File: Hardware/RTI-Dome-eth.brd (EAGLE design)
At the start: 119.4 x 71.1 mm, 87 parts, among them IC1 24AA128ST, IC3 FT232RL, IC4 REG1117, IC5 74LVC245, IC6 74ABT245, J1 POWERPOLE_POWER45A, U1 W5500, X13 PN61729-S, X9 J1011F21PNL

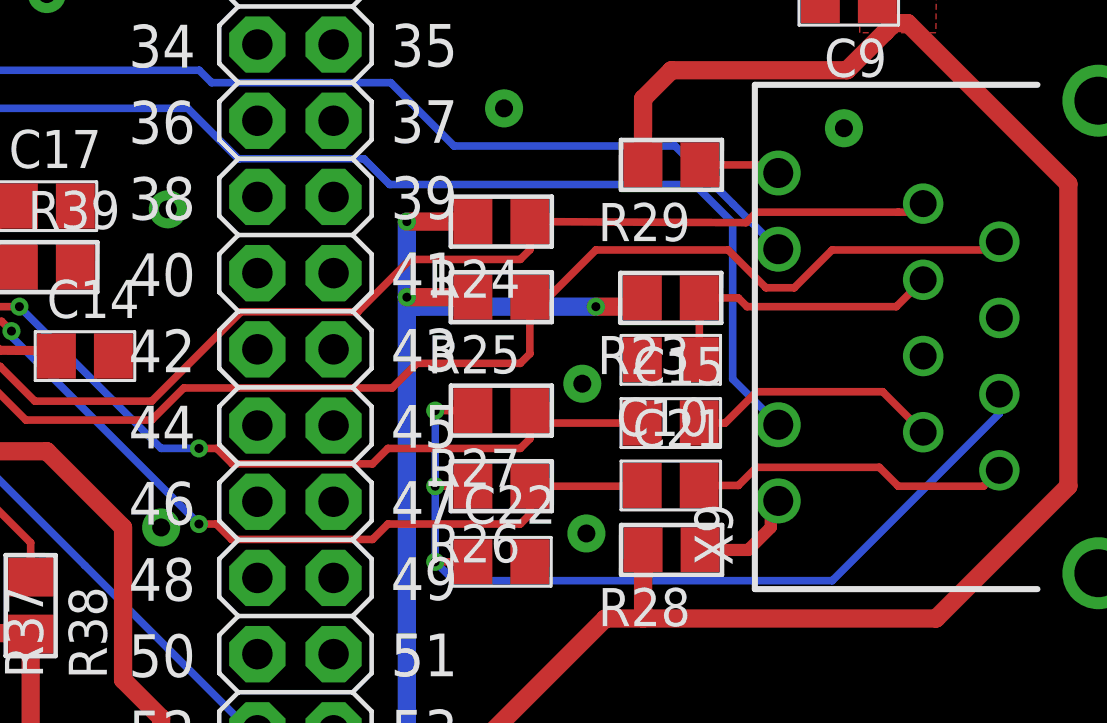
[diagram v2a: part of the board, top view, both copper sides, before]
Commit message: Differential pair are now closer to be the same length.
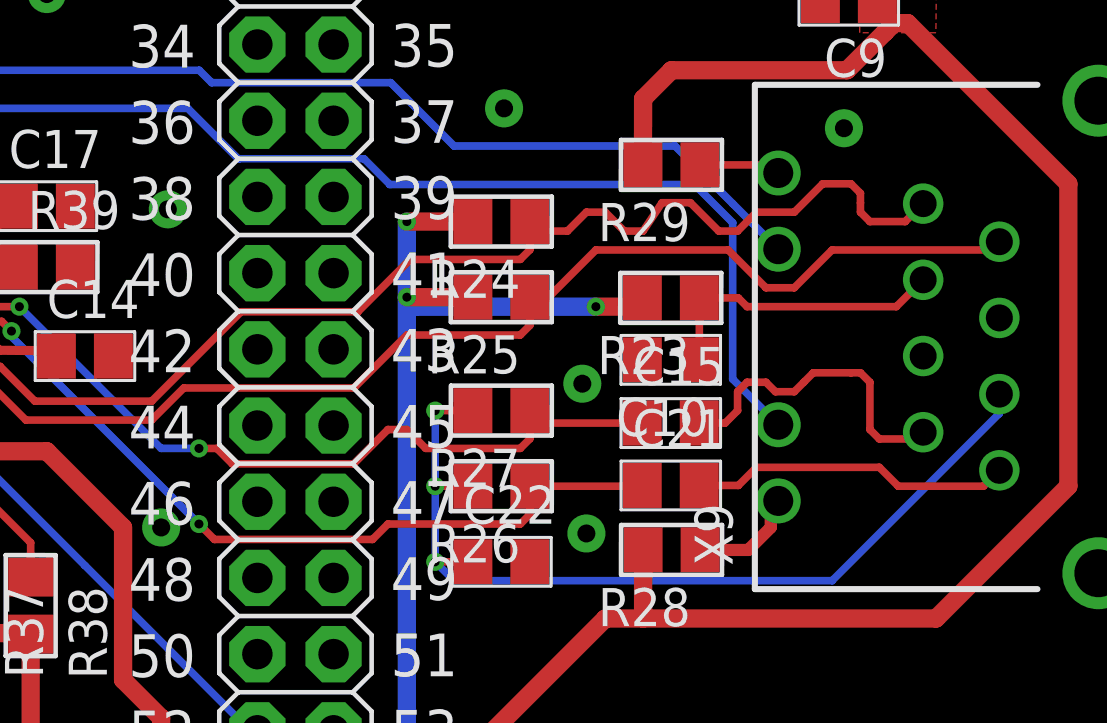
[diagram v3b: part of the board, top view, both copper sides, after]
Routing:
- net TXP: track 36.4 -> 39.4 mm
- net N$11: track 8.46 -> 10.7 mm
- net TXN: track 40.3 -> 39.7 mm
- net RXP: track 26.8 -> 27.4 mm
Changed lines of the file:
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@@
 <wire x1="102.375" y1="34.65" x2="107.675" y2="34.65" width="0.254" layer="1"/>
 <wire x1="107.675" y1="34.65" x2="107.95" y2="34.925" width="0.254" layer="1"/>
-<wire x1="92.3" y1="33.075" x2="92.3" y2="31.19" width="0.254" layer="1"/>
-<wire x1="92.3" y1="31.19" x2="91.98" y2="30.87" width="0.254" layer="1"/>
-<wire x1="91.98" y1="30.87" x2="88.53" y2="30.87" width="0.254" layer="1"/>
-<wire x1="88.53" y1="30.87" x2="87.71" y2="30.05" width="0.254" layer="1"/>
-<wire x1="87.71" y1="30.05" x2="80.765" y2="30.05" width="0.254" layer="1"/>
+<wire x1="86.45" y1="30.05" x2="80.765" y2="30.05" width="0.254" layer="1"/>
 <wire x1="80.765" y1="30.05" x2="79.695" y2="28.98" width="0.254" layer="1"/>
 <wire x1="79.695" y1="28.98" x2="75.5" y2="28.98" width="0.254" layer="1"/>
@@
 <wire x1="74.23" y1="30.25" x2="72.85" y2="30.25" width="0.254" layer="1"/>
 <wire x1="72.85" y1="30.25" x2="72.83" y2="30.27" width="0.254" layer="1"/>
+<wire x1="92.3" y1="33.075" x2="92.3" y2="32.135" width="0.254" layer="1"/>
+<wire x1="92.3" y1="32.135" x2="91.98" y2="31.815" width="0.254" layer="1"/>
+<wire x1="91.98" y1="31.815" x2="88.2" y2="31.815" width="0.254" layer="1"/>
+<wire x1="86.45" y1="30.05" x2="86.45" y2="30.065" width="0.254" layer="1"/>
+<wire x1="86.45" y1="30.065" x2="88.2" y2="31.815" width="0.254" layer="1"/>
 </signal>
 <signal name="RXP">
@@
 <wire x1="92.3" y1="29.295" x2="92.3" y2="28.355" width="0.254" layer="1"/>
 <wire x1="92.3" y1="28.355" x2="91.98" y2="28.035" width="0.254" layer="1"/>
-<wire x1="91.98" y1="28.035" x2="87.57" y2="28.035" width="0.254" layer="1"/>
 <via x="81.27" y="28.035" extent="1-16" drill="0.3"/>
 <wire x1="81.27" y1="28.035" x2="80.01" y2="28.035" width="0.254" layer="16"/>
@@
 <wire x1="75.285" y1="32.76" x2="72.84" y2="32.76" width="0.254" layer="1"/>
 <wire x1="72.84" y1="32.76" x2="72.83" y2="32.77" width="0.254" layer="1"/>
-<wire x1="87.57" y1="28.035" x2="87.055" y2="27.52" width="0.254" layer="1"/>
-<wire x1="87.055" y1="27.52" x2="82.38" y2="27.52" width="0.254" layer="1"/>
+<wire x1="86.425" y1="27.52" x2="82.38" y2="27.52" width="0.254" layer="1"/>
 <wire x1="82.38" y1="27.52" x2="81.865" y2="28.035" width="0.254" layer="1"/>
 <wire x1="81.865" y1="28.035" x2="81.27" y2="28.035" width="0.254" layer="1"/>
+<wire x1="86.425" y1="27.52" x2="87.57" y2="28.665" width="0.254" layer="1"/>
+<wire x1="87.57" y1="28.665" x2="88.2" y2="28.665" width="0.254" layer="1"/>
+<wire x1="88.2" y1="28.665" x2="88.83" y2="28.035" width="0.254" layer="1"/>
+<wire x1="88.83" y1="28.035" x2="91.98" y2="28.035" width="0.254" layer="1"/>
 </signal>
 <signal name="RXN">
@@
 <wire x1="87.57" y1="25.515" x2="87.055" y2="25" width="0.254" layer="1"/>
 <wire x1="87.055" y1="25" x2="82.36" y2="25" width="0.254" layer="1"/>
-<wire x1="82.36" y1="25" x2="81.845" y2="25.515" width="0.254" layer="1"/>
-<wire x1="81.845" y1="25.515" x2="81.27" y2="25.515" width="0.254" layer="1"/>
 <wire x1="75.02" y1="31.945" x2="75.02" y2="31.765" width="0.254" layer="16"/>
 <wire x1="75.02" y1="31.765" x2="81.27" y2="25.515" width="0.254" layer="16"/>
+<wire x1="81.27" y1="25.515" x2="81.785" y2="25" width="0.254" layer="1"/>
+<wire x1="81.785" y1="25" x2="82.36" y2="25" width="0.254" layer="1"/>
 </signal>
 <signal name="TXP">
@@
 <contactref element="X9" pad="1"/>
 <contactref element="R24" pad="1"/>
-<wire x1="92.3" y1="35.595" x2="99.505" y2="35.56" width="0.254" layer="1"/>
-<wire x1="104.58" y1="35.91" x2="99.855" y2="35.91" width="0.254" layer="1"/>
-<wire x1="99.855" y1="35.91" x2="99.505" y2="35.56" width="0.254" layer="1"/>
-<wire x1="104.58" y1="35.91" x2="105.125" y2="35.91" width="0.254" layer="1"/>
-<wire x1="105.125" y1="35.91" x2="105.41" y2="36.195" width="0.254" layer="1"/>
 <wire x1="92.3" y1="35.595" x2="92.3" y2="34.655" width="0.254" layer="1"/>
 <wire x1="92.3" y1="34.655" x2="91.98" y2="34.335" width="0.254" layer="1"/>
@@
 <wire x1="75.8" y1="29.61" x2="74.64" y2="30.77" width="0.254" layer="1"/>
 <wire x1="74.64" y1="30.77" x2="72.83" y2="30.77" width="0.254" layer="1"/>
+<wire x1="99.855" y1="35.91" x2="99.225" y2="35.28" width="0.254" layer="1"/>
+<wire x1="99.225" y1="35.28" x2="98.595" y2="35.28" width="0.254" layer="1"/>
+<wire x1="98.595" y1="35.28" x2="97.65" y2="36.225" width="0.254" layer="1"/>
+<wire x1="99.855" y1="35.91" x2="101.115" y2="35.91" width="0.254" layer="1"/>
+<wire x1="101.115" y1="35.91" x2="102.06" y2="36.855" width="0.254" layer="1"/>
+<wire x1="102.06" y1="36.855" x2="103.005" y2="36.855" width="0.254" layer="1"/>
+<wire x1="103.005" y1="36.855" x2="103.32" y2="36.54" width="0.254" layer="1"/>
+<wire x1="103.32" y1="36.54" x2="103.32" y2="36.225" width="0.254" layer="1"/>
+<wire x1="97.65" y1="36.225" x2="96.705" y2="36.225" width="0.254" layer="1"/>
+<wire x1="96.705" y1="36.225" x2="96.075" y2="35.28" width="0.254" layer="1"/>
+<wire x1="96.075" y1="35.28" x2="95.445" y2="35.28" width="0.254" layer="1"/>
+<wire x1="95.445" y1="35.28" x2="94.815" y2="35.91" width="0.254" layer="1"/>
+<wire x1="94.815" y1="35.91" x2="94.185" y2="35.91" width="0.254" layer="1"/>
+<wire x1="94.185" y1="35.91" x2="93.555" y2="35.28" width="0.254" layer="1"/>
+<wire x1="93.555" y1="35.28" x2="92.615" y2="35.28" width="0.254" layer="1"/>
+<wire x1="92.615" y1="35.28" x2="92.3" y2="35.595" width="0.254" layer="1"/>
+<wire x1="103.32" y1="36.225" x2="103.32" y2="35.91" width="0.254" layer="1"/>
+<wire x1="103.32" y1="35.91" x2="103.635" y2="35.595" width="0.254" layer="1"/>
+<wire x1="103.635" y1="35.595" x2="104.81" y2="35.595" width="0.254" layer="1"/>
+<wire x1="104.81" y1="35.595" x2="105.41" y2="36.195" width="0.254" layer="1"/>
 </signal>
 <signal name="INT_N">
@@
 <contactref element="X9" pad="7"/>
 <contactref element="C15" pad="2"/>
-<wire x1="97.945" y1="28.88" x2="98.81" y2="28.88" width="0.254" layer="1"/>
-<wire x1="98.81" y1="28.88" x2="99.855" y2="29.925" width="0.254" layer="1"/>
-<wire x1="99.855" y1="29.925" x2="104.06" y2="29.925" width="0.254" layer="1"/>
-<wire x1="104.06" y1="29.925" x2="105.41" y2="28.575" width="0.254" layer="1"/>
+<wire x1="103.635" y1="28.665" x2="103.635" y2="30.24" width="0.254" layer="1"/>
+<wire x1="101.43" y1="30.24" x2="101.115" y2="29.925" width="0.254" layer="1"/>
+<wire x1="101.115" y1="29.925" x2="100.485" y2="29.925" width="0.254" layer="1"/>
+<wire x1="100.485" y1="29.925" x2="100.17" y2="30.24" width="0.254" layer="1"/>
+<wire x1="100.17" y1="30.24" x2="99.54" y2="30.24" width="0.254" layer="1"/>
+<wire x1="99.54" y1="30.24" x2="99.225" y2="29.925" width="0.254" layer="1"/>
+<wire x1="99.225" y1="29.925" x2="99.225" y2="29.295" width="0.254" layer="1"/>
+<wire x1="99.225" y1="29.295" x2="98.81" y2="28.88" width="0.254" layer="1"/>
+<wire x1="98.81" y1="28.88" x2="97.945" y2="28.88" width="0.254" layer="1"/>
+<wire x1="101.43" y1="30.24" x2="101.745" y2="30.555" width="0.254" layer="1"/>
+<wire x1="101.745" y1="30.555" x2="103.005" y2="30.555" width="0.254" layer="1"/>
+<wire x1="103.005" y1="30.555" x2="103.32" y2="30.555" width="0.254" layer="1"/>
+<wire x1="103.32" y1="30.555" x2="103.635" y2="30.24" width="0.254" layer="1"/>
+<wire x1="103.635" y1="28.665" x2="103.95" y2="28.35" width="0.254" layer="1"/>
+<wire x1="103.95" y1="28.35" x2="105.185" y2="28.35" width="0.254" layer="1"/>
+<wire x1="105.185" y1="28.35" x2="105.41" y2="28.575" width="0.254" layer="1"/>
 </signal>
 <signal name="N$12">

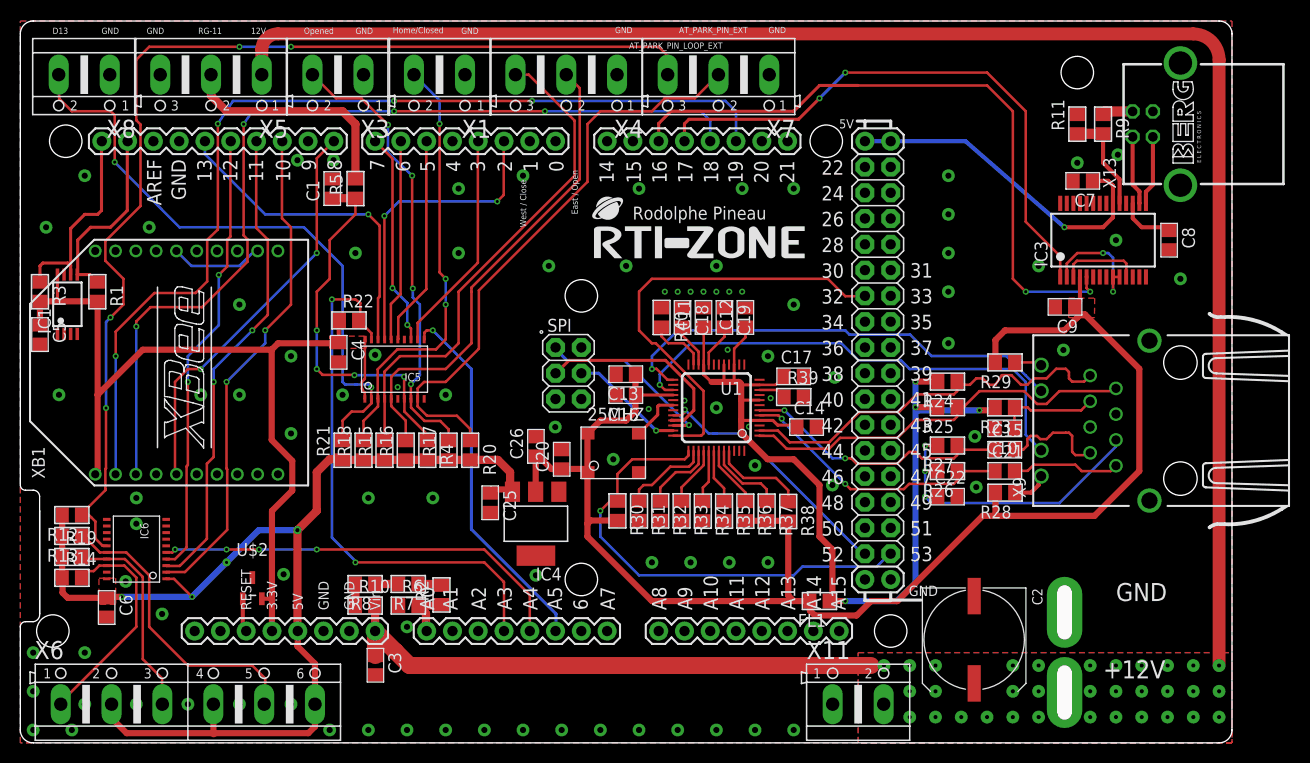
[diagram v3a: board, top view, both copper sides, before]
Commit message: Trace optimisation around the FTDI chip
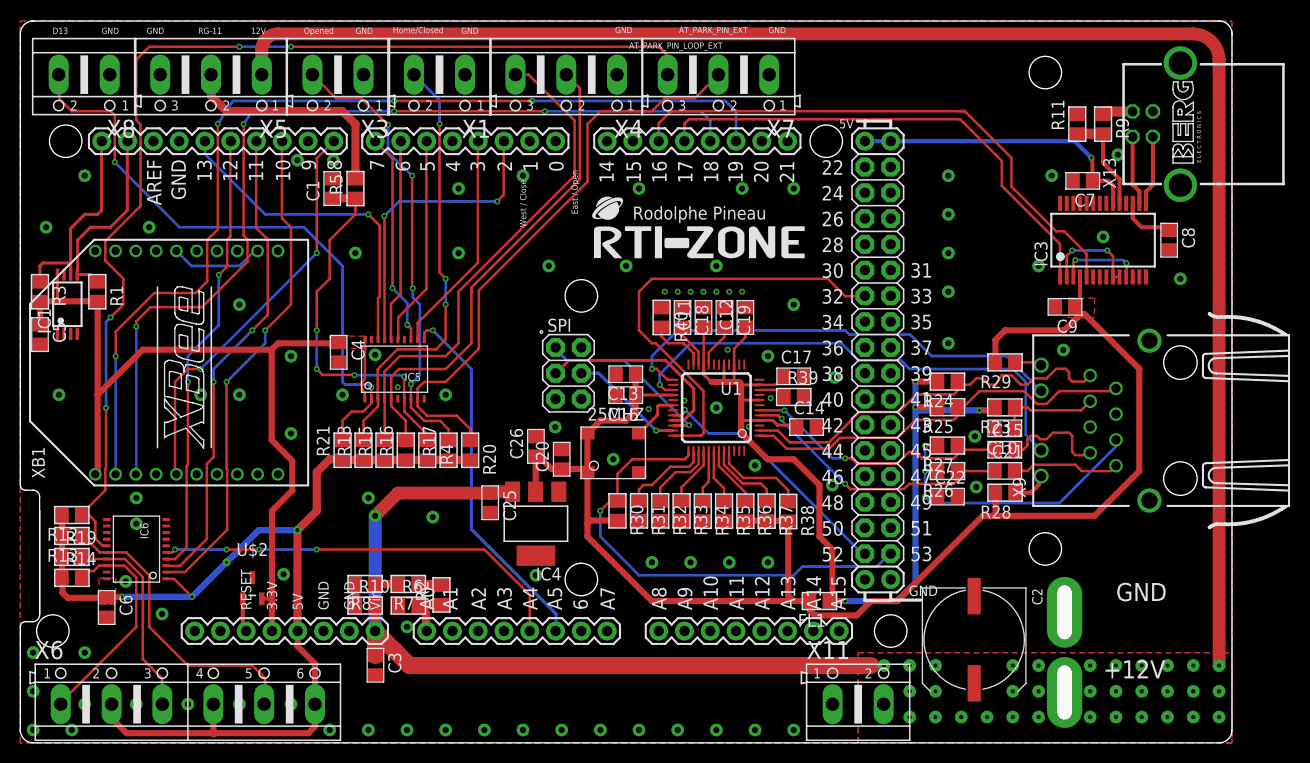
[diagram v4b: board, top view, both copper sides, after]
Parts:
- removed R22: 4.7K, rti:R0805
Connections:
- removed net BUF_EN: IC5.P$19, R22.2, U$1.A3
- net +12V: now also C25.1, IC4.3
- net 3.3V: no longer R22.1
- net GND: now also IC5.P$19
- net VCC: no longer C25.1, IC4.3
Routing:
- net BUF_EN: track 54.2 -> 0.00 mm, vias 2 -> 0
- net +12V: track 213.4 -> 239.2 mm, vias 33 -> 34
- net VCC: track 147.1 -> 134.2 mm
- net TX2: track 65.5 -> 54.2 mm, vias 2 -> 0
- net RX2: track 56.7 -> 48.7 mm, vias 2 -> 0
- net 3.3V: track 92.6 -> 90.3 mm
- net DTR_DSR_DCD: track 11.9 -> 9.77 mm
- net RTS_CTS: track 8.05 -> 8.27 mm, vias 0 -> 2

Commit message: Fix dimention layer on  RTI-Dome-eth.brd, added MPN on all component for mouser.
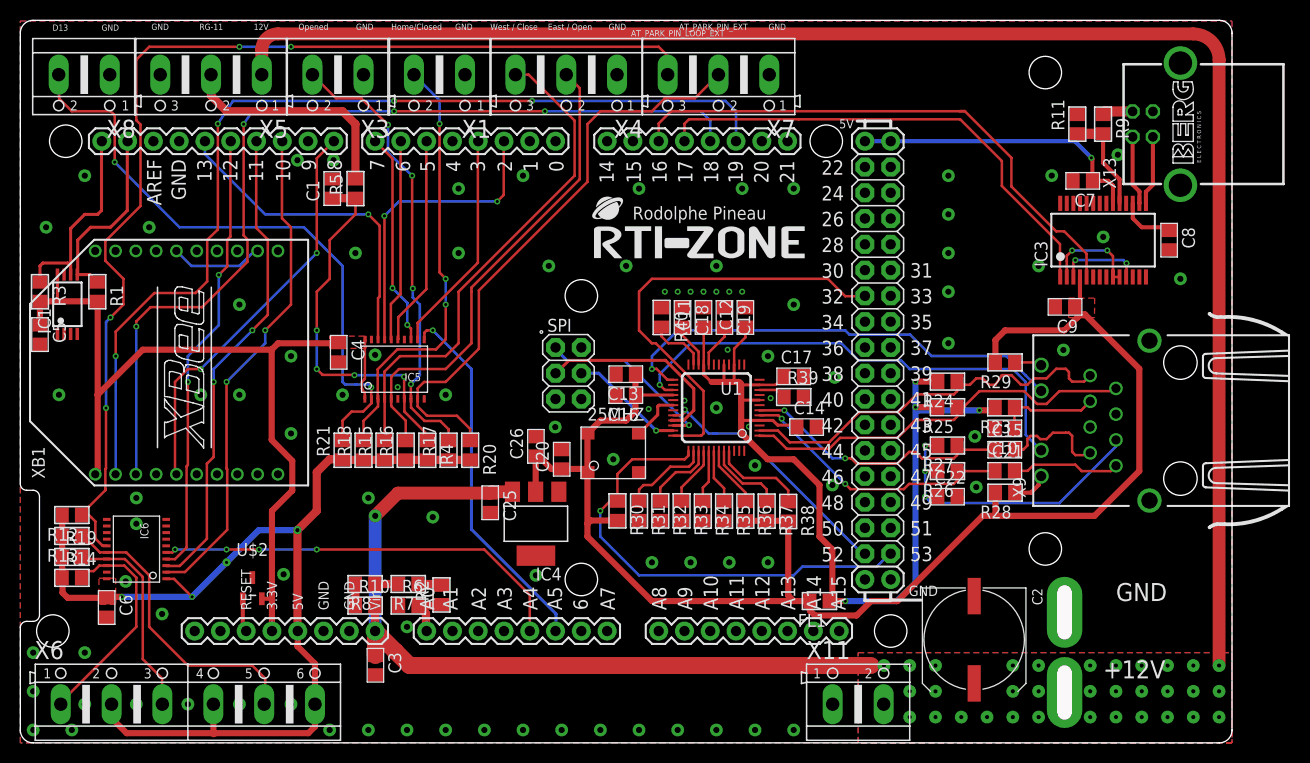
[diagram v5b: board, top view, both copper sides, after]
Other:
- board size 119.4 x 71.1 mm -> 119.4 x 71.2 mm
